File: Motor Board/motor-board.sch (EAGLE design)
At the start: 11 parts

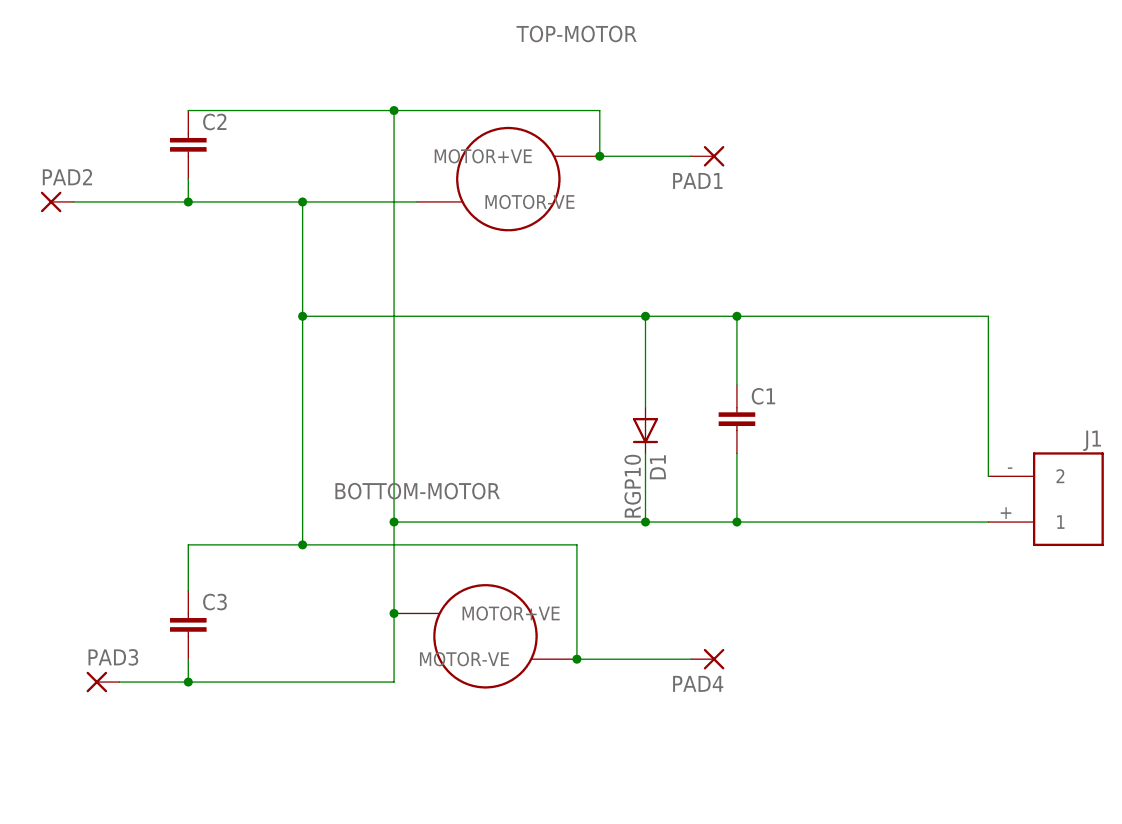
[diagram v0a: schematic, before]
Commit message: Board Update
Redefined 130 motor can and updated board to add solder pads if not using XT60 connectors
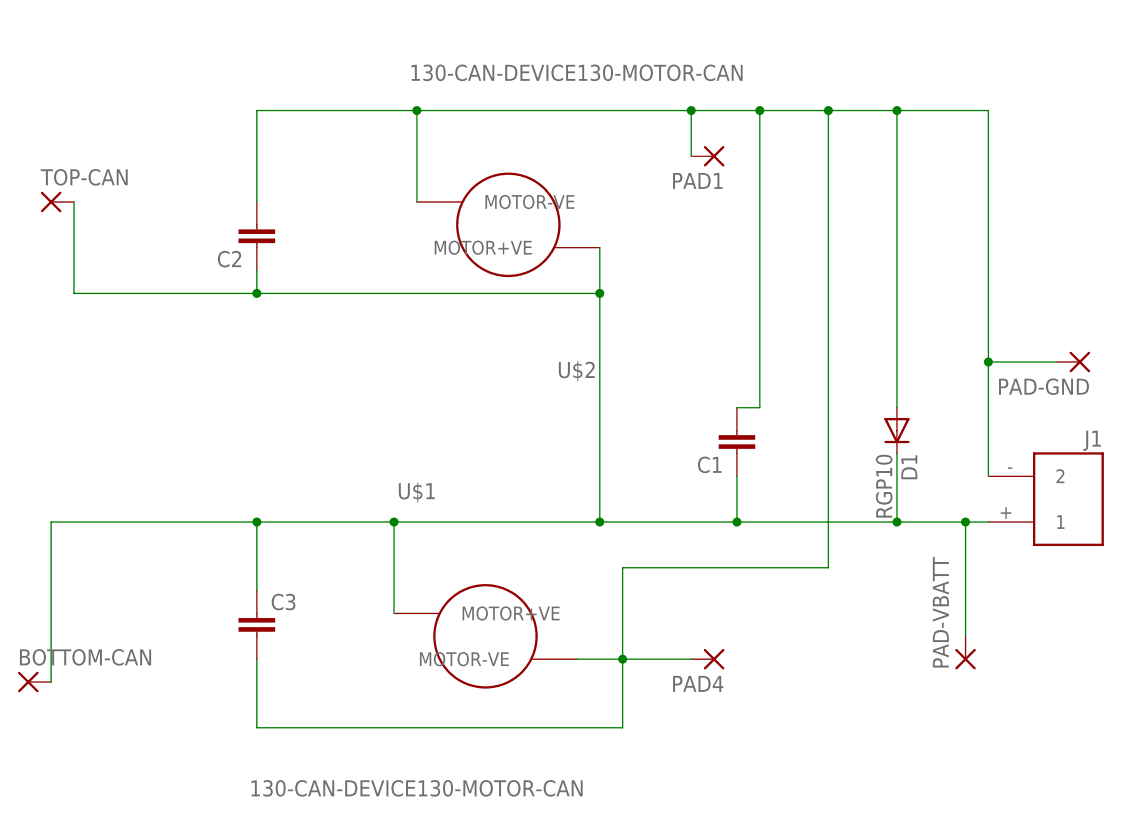
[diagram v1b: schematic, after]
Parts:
- removed PAD3: WIREPADSMD1,27-254, wirepad:WIREPADSMD1,27-254
- removed TOP-MOTOR: 130-CAN-DEVICE130-MOTOR-CAN, 130-can:130-CAN-DEVICE130-MOTOR-CAN
- added BOTTOM-CAN: WIREPADSMD1,27-254, wirepad:WIREPADSMD1,27-254
- added PAD-GND, PAD-VBATT: WIREPAD3,81/1,4, wirepad:WIREPAD3,81/1,4
- added U$2: 130-CAN-DEVICE130-MOTOR-CAN, 130-can:130-CAN-DEVICE130-MOTOR-CAN
- renumbered BOTTOM-MOTOR to U$1, PAD2 to TOP-CAN
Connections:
- net GND: now also C1.2, C3.2, PAD-GND.P, PAD1.P, U$2.MOTOR-VE; no longer C1.1, C3.1, TOP-CAN.P, TOP-MOTOR.MOTOR-VE
- net VBATT: now also BOTTOM-CAN.P, C1.1, C3.1, PAD-VBATT.P, TOP-CAN.P, U$2.MOTOR+VE; no longer C1.2, C3.2, PAD1.P, PAD3.P, TOP-MOTOR.MOTOR+VE
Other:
- moved on the sheet: C1, C2, C3, D1

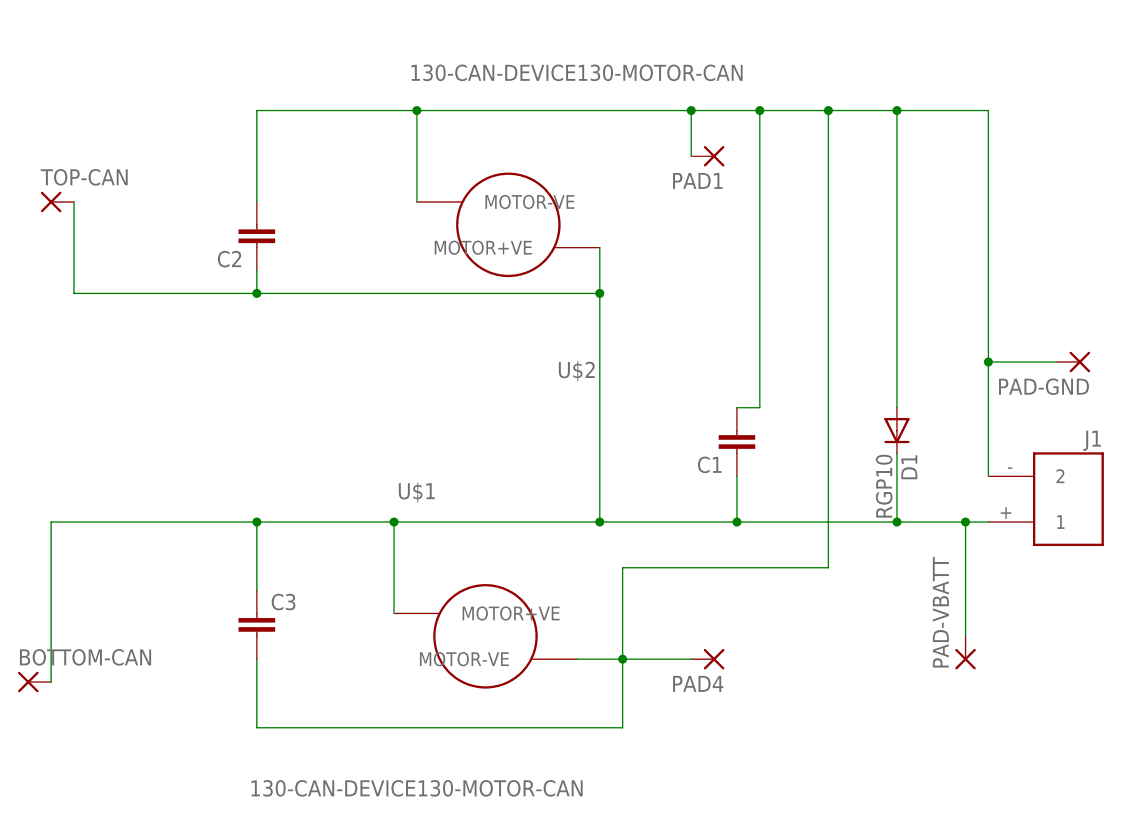
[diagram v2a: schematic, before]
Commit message: Motor Board Update
16mm Gap and some other changes
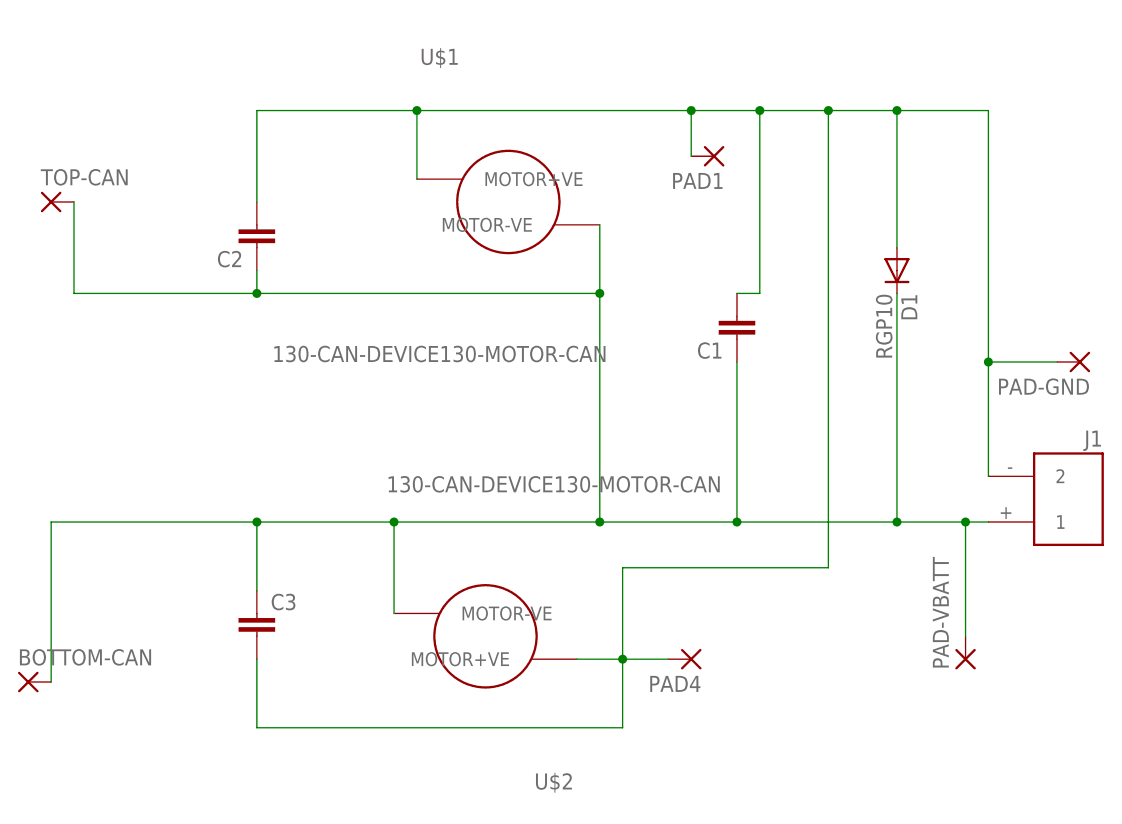
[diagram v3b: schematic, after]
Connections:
- net GND: now also U$1.MOTOR+VE, U$2.MOTOR+VE; no longer U$1.MOTOR-VE, U$2.MOTOR-VE
- net VBATT: now also U$1.MOTOR-VE, U$2.MOTOR-VE; no longer U$1.MOTOR+VE, U$2.MOTOR+VE
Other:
- moved on the sheet: C1, D1, PAD4, U$1, U$2
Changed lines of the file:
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@@
 <part name="BOTTOM-CAN" library="wirepad" deviceset="WIREPAD" device="SMD1,27-254" value=""/>
 <part name="PAD4" library="wirepad" deviceset="WIREPAD" device="SMD1,27-254" value=""/>
+<part name="PAD-GND" library="wirepad" deviceset="WIREPAD" device="3,81/1,4" value=""/>
+<part name="PAD-VBATT" library="wirepad" deviceset="WIREPAD" device="3,81/1,4" value=""/>
 <part name="U$1" library="130-can" deviceset="130-CAN-DEVICE" device="130-MOTOR-CAN"/>
 <part name="U$2" library="130-can" deviceset="130-CAN-DEVICE" device="130-MOTOR-CAN"/>
-<part name="PAD-GND" library="wirepad" deviceset="WIREPAD" device="3,81/1,4" value=""/>
-<part name="PAD-VBATT" library="wirepad" deviceset="WIREPAD" device="3,81/1,4" value=""/>
 </parts>
 <sheets>
@@
 <instances>
 <instance part="J1" gate="G$1" x="101.6" y="38.1" rot="R180"/>
-<instance part="C1" gate="G$1" x="68.58" y="43.18" rot="R180"/>
-<instance part="D1" gate="1" x="86.36" y="45.72" rot="R270"/>
+<instance part="C1" gate="G$1" x="68.58" y="55.88" rot="R180"/>
+<instance part="D1" gate="1" x="86.36" y="63.5" rot="R270"/>
 <instance part="C2" gate="G$1" x="15.24" y="66.04" rot="R180"/>
 <instance part="C3" gate="G$1" x="15.24" y="25.4"/>
@@
 <instance part="TOP-CAN" gate="G$1" x="-7.62" y="71.12"/>
 <instance part="BOTTOM-CAN" gate="G$1" x="-10.16" y="17.78"/>
-<instance part="PAD4" gate="G$1" x="66.04" y="20.32" rot="R180"/>
-<instance part="U$1" gate="G$1" x="40.64" y="22.86"/>
-<instance part="U$2" gate="G$1" x="43.18" y="68.58" rot="R180"/>
+<instance part="PAD4" gate="G$1" x="63.5" y="20.32" rot="R180"/>
 <instance part="PAD-GND" gate="G$1" x="106.68" y="53.34" rot="R180"/>
 <instance part="PAD-VBATT" gate="G$1" x="93.98" y="20.32" rot="R90"/>
+<instance part="U$1" gate="G$1" x="43.18" y="71.12"/>
+<instance part="U$2" gate="G$1" x="40.64" y="22.86" rot="R180"/>
 </instances>
 <busses>
@@
 <segment>
 <pinref part="J1" gate="G$1" pin="1"/>
-<pinref part="U$1" gate="G$1" pin="MOTOR+VE"/>
 <wire x1="96.52" y1="35.56" x2="93.98" y2="35.56" width="0.1524" layer="91"/>
 <wire x1="93.98" y1="35.56" x2="86.36" y2="35.56" width="0.1524" layer="91"/>
@@
 <wire x1="68.58" y1="35.56" x2="53.34" y2="35.56" width="0.1524" layer="91"/>
 <wire x1="53.34" y1="35.56" x2="30.48" y2="35.56" width="0.1524" layer="91"/>
-<wire x1="30.48" y1="35.56" x2="30.48" y2="25.4" width="0.1524" layer="91"/>
-<pinref part="U$2" gate="G$1" pin="MOTOR+VE"/>
 <junction x="53.34" y="35.56"/>
 <pinref part="C1" gate="G$1" pin="1"/>
-<wire x1="53.34" y1="66.04" x2="53.34" y2="60.96" width="0.1524" layer="91"/>
+<wire x1="30.48" y1="35.56" x2="15.24" y2="35.56" width="0.1524" layer="91"/>
 <wire x1="53.34" y1="60.96" x2="53.34" y2="35.56" width="0.1524" layer="91"/>
-<wire x1="68.58" y1="35.56" x2="68.58" y2="40.64" width="0.1524" layer="91"/>
+<wire x1="68.58" y1="35.56" x2="68.58" y2="53.34" width="0.1524" layer="91"/>
 <junction x="68.58" y="35.56"/>
 <pinref part="C2" gate="G$1" pin="1"/>
 <wire x1="53.34" y1="60.96" x2="15.24" y2="60.96" width="0.1524" layer="91"/>
 <wire x1="15.24" y1="60.96" x2="15.24" y2="63.5" width="0.1524" layer="91"/>
-<junction x="53.34" y="60.96"/>
 <pinref part="C3" gate="G$1" pin="1"/>
-<wire x1="30.48" y1="35.56" x2="15.24" y2="35.56" width="0.1524" layer="91"/>
 <wire x1="15.24" y1="35.56" x2="15.24" y2="27.94" width="0.1524" layer="91"/>
-<junction x="30.48" y="35.56"/>
 <pinref part="BOTTOM-CAN" gate="G$1" pin="P"/>
 <wire x1="15.24" y1="35.56" x2="-7.62" y2="35.56" width="0.1524" layer="91"/>
@@
 <junction x="15.24" y="60.96"/>
 <pinref part="D1" gate="1" pin="C"/>
-<wire x1="86.36" y1="43.18" x2="86.36" y2="35.56" width="0.1524" layer="91"/>
+<wire x1="86.36" y1="60.96" x2="86.36" y2="35.56" width="0.1524" layer="91"/>
 <junction x="86.36" y="35.56"/>
 <pinref part="PAD-VBATT" gate="G$1" pin="P"/>
 <wire x1="93.98" y1="22.86" x2="93.98" y2="35.56" width="0.1524" layer="91"/>
 <junction x="93.98" y="35.56"/>
+<pinref part="U$2" gate="G$1" pin="MOTOR-VE"/>
+<wire x1="30.48" y1="25.4" x2="30.48" y2="35.56" width="0.1524" layer="91"/>
+<junction x="30.48" y="35.56"/>
+<pinref part="U$1" gate="G$1" pin="MOTOR-VE"/>
+<wire x1="53.34" y1="60.96" x2="53.34" y2="68.58" width="0.1524" layer="91"/>
+<junction x="53.34" y="60.96"/>
 </segment>
 </net>
 <net name="GND" class="0">
 <segment>
-<pinref part="U$2" gate="G$1" pin="MOTOR-VE"/>
-<wire x1="33.02" y1="71.12" x2="33.02" y2="81.28" width="0.1524" layer="91"/>
 <pinref part="J1" gate="G$1" pin="2"/>
+<wire x1="15.24" y1="81.28" x2="33.02" y2="81.28" width="0.1524" layer="91"/>
 <wire x1="33.02" y1="81.28" x2="63.5" y2="81.28" width="0.1524" layer="91"/>
 <wire x1="63.5" y1="81.28" x2="71.12" y2="81.28" width="0.1524" layer="91"/>
@@
 <wire x1="86.36" y1="81.28" x2="96.52" y2="81.28" width="0.1524" layer="91"/>
 <wire x1="96.52" y1="81.28" x2="96.52" y2="53.34" width="0.1524" layer="91"/>
-<pinref part="U$1" gate="G$1" pin="MOTOR-VE"/>
 <wire x1="96.52" y1="53.34" x2="96.52" y2="40.64" width="0.1524" layer="91"/>
-<wire x1="50.8" y1="20.32" x2="55.88" y2="20.32" width="0.1524" layer="91"/>
 <wire x1="55.88" y1="20.32" x2="55.88" y2="30.48" width="0.1524" layer="91"/>
 <wire x1="55.88" y1="30.48" x2="78.74" y2="30.48" width="0.1524" layer="91"/>
@@
 <junction x="78.74" y="81.28"/>
 <pinref part="C1" gate="G$1" pin="2"/>
-<wire x1="68.58" y1="48.26" x2="71.12" y2="48.26" width="0.1524" layer="91"/>
-<wire x1="71.12" y1="48.26" x2="71.12" y2="81.28" width="0.1524" layer="91"/>
+<wire x1="68.58" y1="60.96" x2="71.12" y2="60.96" width="0.1524" layer="91"/>
+<wire x1="71.12" y1="60.96" x2="71.12" y2="81.28" width="0.1524" layer="91"/>
 <junction x="71.12" y="81.28"/>
 <pinref part="C2" gate="G$1" pin="2"/>
-<wire x1="33.02" y1="81.28" x2="15.24" y2="81.28" width="0.1524" layer="91"/>
 <wire x1="15.24" y1="81.28" x2="15.24" y2="71.12" width="0.1524" layer="91"/>
-<junction x="33.02" y="81.28"/>
 <pinref part="C3" gate="G$1" pin="2"/>
 <wire x1="15.24" y1="20.32" x2="15.24" y2="12.7" width="0.1524" layer="91"/>
@@
 <junction x="55.88" y="20.32"/>
 <pinref part="PAD4" gate="G$1" pin="P"/>
-<wire x1="63.5" y1="20.32" x2="55.88" y2="20.32" width="0.1524" layer="91"/>
 <pinref part="PAD1" gate="G$1" pin="P"/>
+<wire x1="60.96" y1="20.32" x2="55.88" y2="20.32" width="0.1524" layer="91"/>
 <wire x1="63.5" y1="76.2" x2="63.5" y2="81.28" width="0.1524" layer="91"/>
 <junction x="63.5" y="81.28"/>
 <pinref part="D1" gate="1" pin="A"/>
-<wire x1="86.36" y1="48.26" x2="86.36" y2="81.28" width="0.1524" layer="91"/>
+<wire x1="86.36" y1="66.04" x2="86.36" y2="81.28" width="0.1524" layer="91"/>
 <junction x="86.36" y="81.28"/>
 <pinref part="PAD-GND" gate="G$1" pin="P"/>
 <wire x1="104.14" y1="53.34" x2="96.52" y2="53.34" width="0.1524" layer="91"/>
 <junction x="96.52" y="53.34"/>
+<pinref part="U$2" gate="G$1" pin="MOTOR+VE"/>
+<wire x1="50.8" y1="20.32" x2="55.88" y2="20.32" width="0.1524" layer="91"/>
+<pinref part="U$1" gate="G$1" pin="MOTOR+VE"/>
+<wire x1="33.02" y1="73.66" x2="33.02" y2="81.28" width="0.1524" layer="91"/>
+<junction x="33.02" y="81.28"/>
 </segment>
 </net>
